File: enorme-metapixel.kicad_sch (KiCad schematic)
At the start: 31 parts, among them J1 VIN, J2 STRIP_0, J3 STRIP_1, J4 STRIP_2, J5 UART, J6 VIN, SW1 SW_RESET, SW2 SW_BOOT, U1 BD33FC0FP, U2 ESP32-WROOM-32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

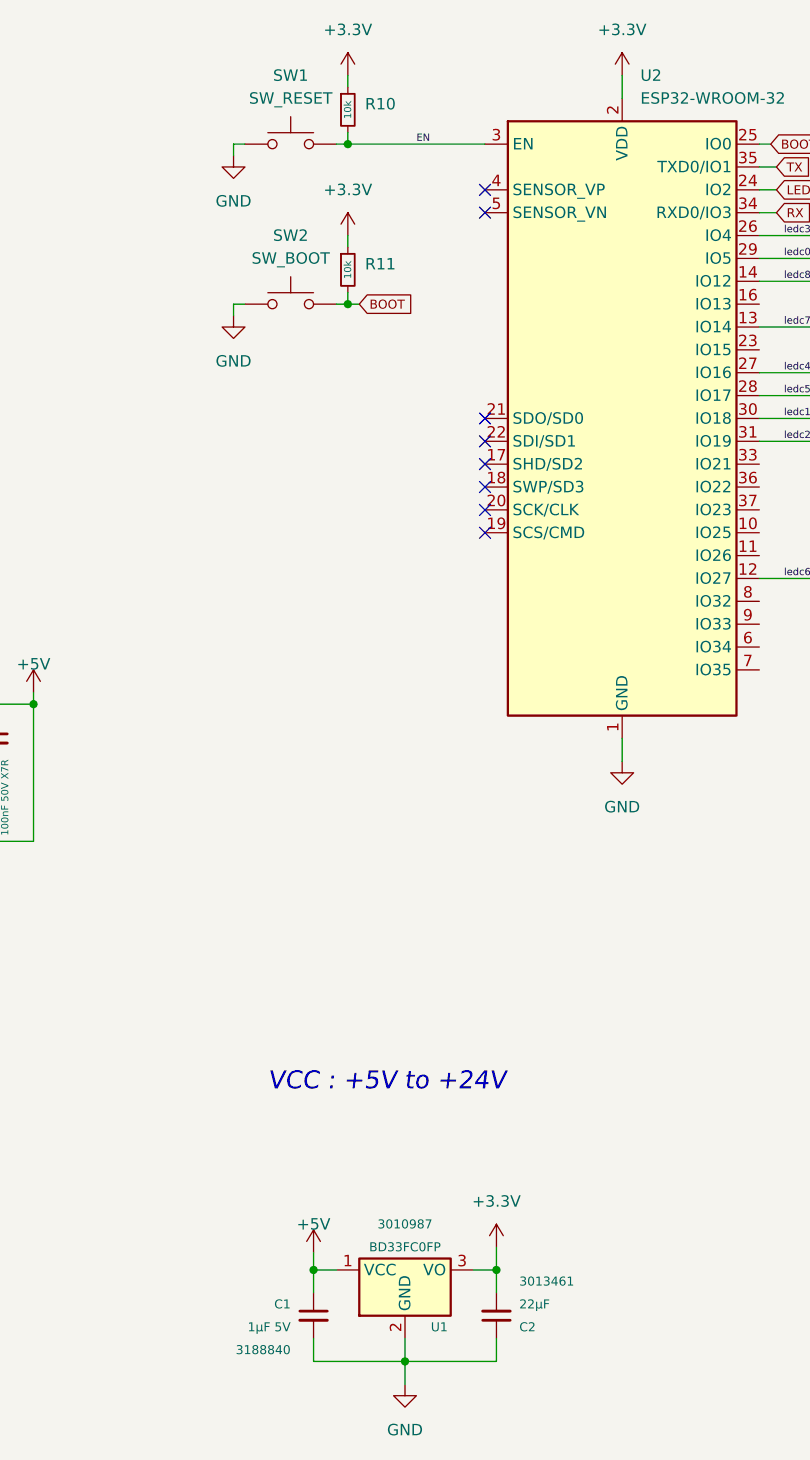
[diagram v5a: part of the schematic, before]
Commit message: Fix comp refs, replace LDO with easier one easier to get
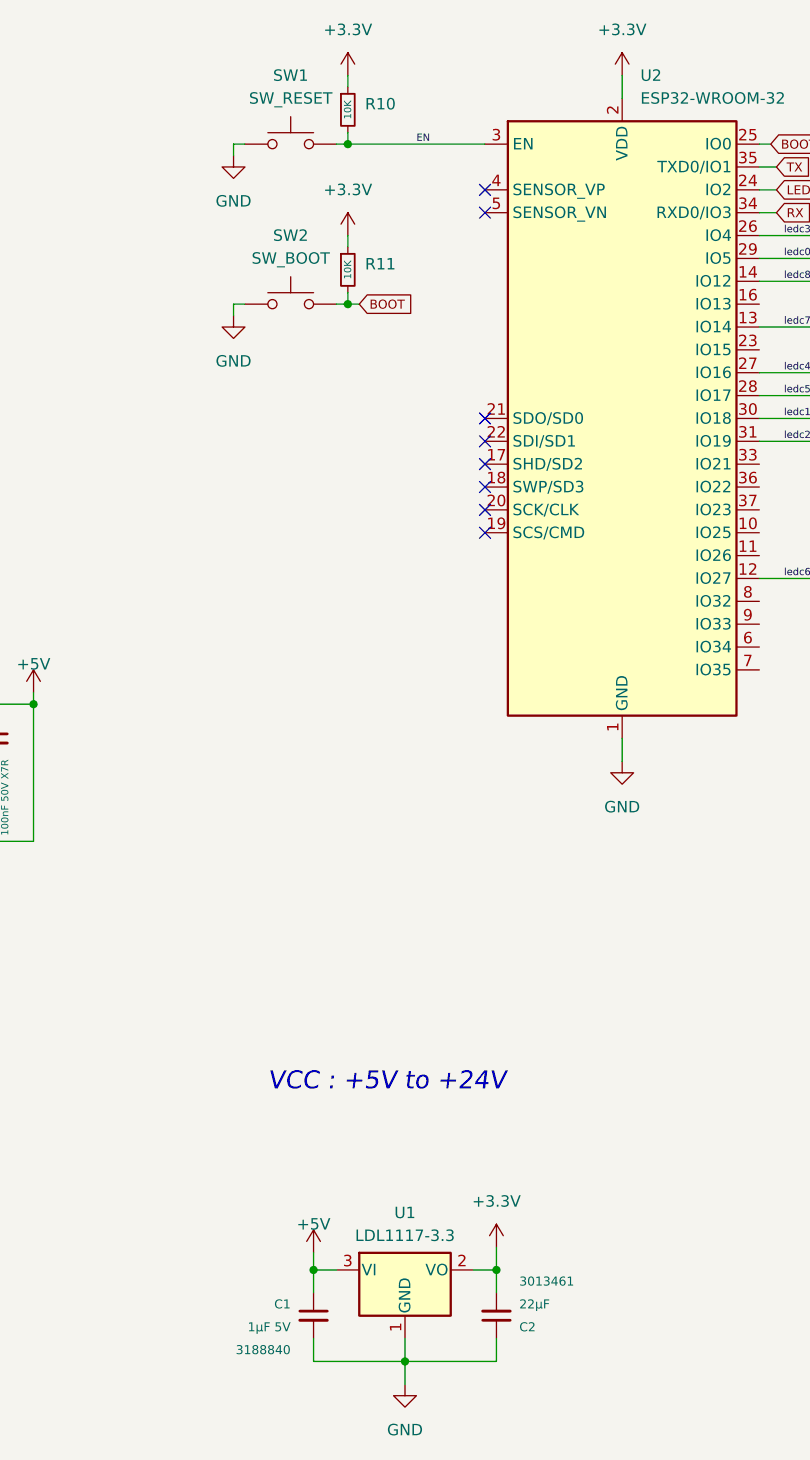
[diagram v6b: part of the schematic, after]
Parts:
- removed U1: BD33FC0FP, Package_TO_SOT_SMD:TO-252-2, symbol Regulator_Linear:BD33FC0FP
- added U1: LDL1117-3.3, Package_TO_SOT_SMD:SOT-223-3_TabPin2, symbol Regulator_Linear:AZ1117-3.3
- C2: LCSC (none) -> C7432770
- D1: LCSC (none) -> C965807; MFR (none) -> XL-1608UBC-04
- H1, H2, J1, J2, J3, J4, J5, J6: MFR (none) -> do not place
- L1: MFR (none) -> CYA0650-6.8UH
- R10, R11: value 10k -> 10K
- SW1, SW2: LCSC (none) -> C701204; MFR (none) -> EVQQ2U03W
- U2: LCSC (none) -> C82899; MFR (none) -> ESP32-WROOM-32-N4
- U3: MFR (none) -> TPS62933DRLR
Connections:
- net +3.3V: now also U1.2 (VO)
- net +5V: now also U1.3 (VI)
- net GND: now also U1.1 (GND)
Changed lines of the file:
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@@
       (effects (font (size 1.27 1.27)) (justify left))
     )
-    (property "Value" "10k" (at 147.955 43.815 90)
+    (property "Value" "10K" (at 147.955 43.815 90)
       (effects (font (size 0.8 0.8)))
     )
@@
       (effects (font (size 1.27 1.27)) hide)
     )
+    (property "MFR" "" (at 147.955 43.815 0)
+      (effects (font (size 1.27 1.27)) hide)
+    )
     (pin "1")
     (pin "2")
@@
     )
     (property "Datasheet" "~" (at 269.24 36.83 0)
+      (effects (font (size 1.27 1.27)) hide)
+    )
+    (property "MFR" "do not place" (at 269.24 36.83 0)
       (effects (font (size 1.27 1.27)) hide)
     )
@@
       (effects (font (size 1.27 1.27)) hide)
     )
+    (property "MFR" "" (at 220.98 149.86 0)
+      (effects (font (size 1.27 1.27)) hide)
+    )
     (pin "1")
     (pin "2")
@@
       (effects (font (size 1.27 1.27)) (justify left))
     )
-    (property "Value" "10k" (at 147.955 26.035 90)
+    (property "Value" "10K" (at 147.955 26.035 90)
       (effects (font (size 0.8 0.8)))
     )
@@
       (effects (font (size 1.27 1.27)) hide)
     )
+    (property "MFR" "" (at 147.955 26.035 0)
+      (effects (font (size 1.27 1.27)) hide)
+    )
     (pin "1")
     (pin "2")
@@
     )
     (property "Datasheet" "~" (at 267.97 110.49 0)
+      (effects (font (size 1.27 1.27)) hide)
+    )
+    (property "MFR" "do not place" (at 267.97 110.49 0)
       (effects (font (size 1.27 1.27)) hide)
     )
@@
     )
   )
-  (symbol (lib_id "Regulator_Linear:BD33FC0FP") (at 154.305 154.94 0) (unit 1)
-    (in_bom yes) (on_board yes) (dnp no)
-    (property "Reference" "U1" (at 158.115 161.29 0)
-      (effects (font (size 1 1)))
-    )
-    (property "Value" "BD33FC0FP" (at 154.305 152.4 0)
-      (effects (font (size 1 1)))
-    )
-    (property "Footprint" "Package_TO_SOT_SMD:TO-252-2" (at 154.305 152.4 0)
-      (effects (font (size 1.27 1.27)) hide)
-    )
-    (property "Datasheet" "https://fscdn.rohm.com/en/products/databook/datasheet/ic/power/linear_regulator/bdxxfc0wefj-e.pdf" (at 154.305 144.78 0)
-      (effects (font (size 1.27 1.27)) hide)
-    )
-    (property "Farnell" "3010987" (at 154.305 149.86 0)
-      (effects (font (size 1 1)))
-    )
-    (pin "1")
-    (pin "2")
-    (pin "3")
-    (instances
-      (project "enorme-metapixel"
-        (path "/46cf7f64-ef08-4474-bf51-0f079d0a1dde"
-          (reference "U1") (unit 1)
-        )
-      )
-    )
-  )
   (symbol (lib_id "power:+3.3V") (at 147.955 22.225 0) (unit 1)
     (in_bom yes) (on_board yes) (dnp no) (fields_autoplaced)
@@
     )
     (property "Datasheet" "~" (at 273.05 148.59 0)
+      (effects (font (size 1.27 1.27)) hide)
+    )
+    (property "MFR" "do not place" (at 273.05 148.59 0)
       (effects (font (size 1.27 1.27)) hide)
     )
@@
       (effects (font (size 0.8 0.8)))
     )
+    (property "MFR" "" (at 53.975 106.045 0)
+      (effects (font (size 1.27 1.27)) hide)
+    )
     (pin "1")
     (pin "2")
@@
     )
     (property "Datasheet" "~" (at 17.145 27.94 0)
+      (effects (font (size 1.27 1.27)) hide)
+    )
+    (property "MFR" "do not place" (at 17.145 27.94 0)
       (effects (font (size 1.27 1.27)) hide)
     )
@@
       (effects (font (size 0.8 0.8)))
     )
+    (property "MFR" "" (at 108.585 95.885 0)
+      (effects (font (size 1.27 1.27)) hide)
+    )
     (pin "1")
     (pin "2")
@@
       (effects (font (size 1.27 1.27)) hide)
     )
+    (property "MFR" "XL-1608UBC-04" (at 220.98 143.51 0)
+      (effects (font (size 1.27 1.27)) hide)
+    )
+    (property "LCSC" "C965807" (at 220.98 143.51 0)
+      (effects (font (size 1.27 1.27)) hide)
+    )
     (pin "1")
     (pin "2")
@@
       (effects (font (size 0.87 0.87)))
     )
+    (property "MFR" "" (at 84.455 92.075 0)
+      (effects (font (size 1.27 1.27)) hide)
+    )
     (pin "1")
     (pin "2")
@@
       (effects (font (size 0.8 0.8)))
     )
+    (property "MFR" "" (at 42.545 95.885 0)
+      (effects (font (size 1.27 1.27)) hide)
+    )
     (pin "1")
     (pin "2")
@@
       (effects (font (size 1 1)) (justify right))
     )
+    (property "MFR" "" (at 164.465 160.02 0)
+      (effects (font (size 1.27 1.27)) hide)
+    )
+    (property "LCSC" "C7432770" (at 164.465 160.02 0)
+      (effects (font (size 1.27 1.27)) hide)
+    )
     (pin "1")
     (pin "2")
@@
     )
     (property "Datasheet" "~" (at 267.97 64.77 0)
+      (effects (font (size 1.27 1.27)) hide)
+    )
+    (property "MFR" "do not place" (at 267.97 64.77 0)
       (effects (font (size 1.27 1.27)) hide)
     )
@@
     )
     (property "Datasheet" "https://www.espressif.com/sites/default/files/documentation/esp32-wroom-32_datasheet_en.pdf" (at 170.815 59.055 0)
+      (effects (font (size 1.27 1.27)) hide)
+    )
+    (property "LCSC" "C82899" (at 178.435 60.325 0)
+      (effects (font (size 1.27 1.27)) hide)
+    )
+    (property "MFR" "ESP32-WROOM-32-N4" (at 178.435 60.325 0)
       (effects (font (size 1.27 1.27)) hide)
     )
@@
       (effects (font (size 1.27 1.27)) hide)
     )
+    (property "MFR" "" (at 78.105 107.315 0)
+      (effects (font (size 1.27 1.27)) hide)
+    )
     (pin "1")
     (pin "2")
@@
     )
     (property "Datasheet" "~" (at 273.05 154.94 0)
+      (effects (font (size 1.27 1.27)) hide)
+    )
+    (property "MFR" "do not place" (at 273.05 154.94 0)
       (effects (font (size 1.27 1.27)) hide)
     )
@@
       (effects (font (size 1 1)) (justify right))
     )
+    (property "MFR" "" (at 144.145 160.02 0)
+      (effects (font (size 1.27 1.27)) hide)
+    )
     (pin "1")
     (pin "2")
@@
       (effects (font (size 0.8 0.8)))
     )
+    (property "MFR" "" (at 36.83 95.885 0)
+      (effects (font (size 1.27 1.27)) hide)
+    )
     (pin "1")
     (pin "2")
@@
     )
     (property "Datasheet" "~" (at 141.605 24.765 0)
+      (effects (font (size 1.27 1.27)) hide)
+    )
+    (property "LCSC" "C701204" (at 141.605 29.845 0)
+      (effects (font (size 1.27 1.27)) hide)
+    )
+    (property "MFR" "EVQQ2U03W" (at 141.605 29.845 0)
       (effects (font (size 1.27 1.27)) hide)
     )
@@
       (effects (font (size 0.8 0.8)))
     )
+    (property "MFR" "CYA0650-6.8UH" (at 92.075 92.075 0)
+      (effects (font (size 1.27 1.27)) hide)
+    )
     (pin "1")
     (pin "2")
@@
       (effects (font (size 0.8 0.8)))
     )
+    (property "MFR" "" (at 97.155 95.885 0)
+      (effects (font (size 1.27 1.27)) hide)
+    )
     (pin "1")
     (pin "2")
@@
     )
     (property "Datasheet" "~" (at 141.605 42.545 0)
+      (effects (font (size 1.27 1.27)) hide)
+    )
+    (property "LCSC" "C701204" (at 141.605 47.625 0)
+      (effects (font (size 1.27 1.27)) hide)
+    )
+    (property "MFR" "EVQQ2U03W" (at 141.605 47.625 0)
       (effects (font (size 1.27 1.27)) hide)
     )
@@
       (effects (font (size 1.27 1.27)) hide)
     )
+    (property "MFR" "" (at 76.835 92.075 0)
+      (effects (font (size 1.27 1.27)) hide)
+    )
     (pin "1")
     (pin "2")
@@
     )
     (property "Datasheet" "~" (at 267.97 87.63 0)
+      (effects (font (size 1.27 1.27)) hide)
+    )
+    (property "MFR" "do not place" (at 267.97 87.63 0)
       (effects (font (size 1.27 1.27)) hide)
     )
@@
       (effects (font (size 1.27 1.27)) hide)
     )
+    (property "MFR" "do not place" (at 17.145 48.895 0)
+      (effects (font (size 1.27 1.27)) hide)
+    )
     (pin "1")
     (pin "2")
@@
       (effects (font (size 0.8 0.8)))
     )
+    (property "MFR" "" (at 102.87 95.885 0)
+      (effects (font (size 1.27 1.27)) hide)
+    )
     (pin "1")
     (pin "2")
@@
     (property "LCSC" "C3200405" (at 65.405 88.265 0)
       (effects (font (size 0.89 0.89)))
+    )
+    (property "MFR" "TPS62933DRLR" (at 65.405 99.695 0)
+      (effects (font (size 1.27 1.27)) hide)
     )
     (pin "1")
@@
     )
   )
+  (symbol (lib_id "Regulator_Linear:AZ1117-3.3") (at 154.305 154.94 0) (unit 1)
+    (in_bom yes) (on_board yes) (dnp no) (fields_autoplaced)
+    (property "Reference" "U1" (at 154.305 148.59 0)
+      (effects (font (size 1.27 1.27)))
+    )
+    (property "Value" "LDL1117-3.3" (at 154.305 151.13 0)
+      (effects (font (size 1.27 1.27)))
+    )
+    (property "Footprint" "Package_TO_SOT_SMD:SOT-223-3_TabPin2" (at 154.305 148.59 0)
+      (effects (font (size 1.27 1.27) italic) hide)
+    )
+    (property "Datasheet" "https://www.diodes.com/assets/Datasheets/AZ1117.pdf" (at 154.305 154.94 0)
+      (effects (font (size 1.27 1.27)) hide)
+    )
+    (property "LCSC" "C435835" (at 154.305 154.94 0)
+      (effects (font (size 1.27 1.27)) hide)
+    )
+    (property "MFR" "LDL1117S33R" (at 154.305 154.94 0)
+      (effects (font (size 1.27 1.27)) hide)
+    )
+    (pin "1")
+    (pin "2")
+    (pin "3")
+    (instances
+      (project "enorme-metapixel"
+        (path "/46cf7f64-ef08-4474-bf51-0f079d0a1dde"
+          (reference "U1") (unit 1)
+        )
+      )
+    )
+  )
   (symbol (lib_id "power:GND") (at 24.765 51.435 0) (unit 1)
     (in_bom yes) (on_board yes) (dnp no) (fields_autoplaced)
@@
       (effects (font (size 1.27 1.27)) hide)
     )
+    (property "MFR" "" (at 74.295 111.125 0)
+      (effects (font (size 1.27 1.27)) hide)
+    )
     (pin "1")
     (pin "2")
@@
       (effects (font (size 0.8 0.8)))
     )
-    (pin "1")
+    (property "MFR" "" (at 48.26 95.885 0)
+      (effects (font (size 1.27 1.27)) hide)
+    )
+    (pin "1")
